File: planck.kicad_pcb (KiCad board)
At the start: 2 copper layers, 115 x 75 mm, 134 parts, among them J1 USB_C_U262-161N-4BVC11, J2 USB_C_U262-161N-4BVC11, J3 USB_C_U262-161N-4BVC11, SW1 SW_Hotswap_Kailh_Choc_V1_1u, SW10 SW_Hotswap_Kailh_Choc_V1_1u, SW11 SW_Hotswap_Kailh_Choc_V1_1u, SW12 SW_Hotswap_Kailh_Choc_V1_1u, SW13 SW_Hotswap_Kailh_Choc_V1_1u, SW14 SW_Hotswap_Kailh_Choc_V1_1u, SW15 SW_Hotswap_Kailh_Choc_V1_1u, SW16 SW_Hotswap_Kailh_Choc_V1_1u, SW17 SW_Hotswap_Kailh_Choc_V1_1u, SW18 SW_Hotswap_Kailh_Choc_V1_1u, SW19 SW_Hotswap_Kailh_Choc_V1_1u, SW2 SW_Hotswap_Kailh_Choc_V1_1u, SW20 SW_Hotswap_Kailh_Choc_V1_1u, SW21 SW_Hotswap_Kailh_Choc_V1_1u, SW22 SW_Hotswap_Kailh_Choc_V1_1u, SW23 SW_Hotswap_Kailh_Choc_V1_1u, SW24 SW_Hotswap_Kailh_Choc_V1_1u, SW25 SW_Push, SW3 SW_Hotswap_Kailh_Choc_V1_1u, SW4 SW_Hotswap_Kailh_Choc_V1_1u, SW5 SW_Hotswap_Kailh_Choc_V1_1u, SW6 SW_Hotswap_Kailh_Choc_V1_1u, SW7 SW_Hotswap_Kailh_Choc_V1_1u, SW8 SW_Hotswap_Kailh_Choc_V1_1u, SW9 SW_Hotswap_Kailh_Choc_V1_1u, U1 RP2040 ARM Cortex-M0 133MHz, U2 ME6219C33M5G, U3 W25Q16JVUXIQ, Y1 32MHz ±10ppm 20pF SMD3225-4P

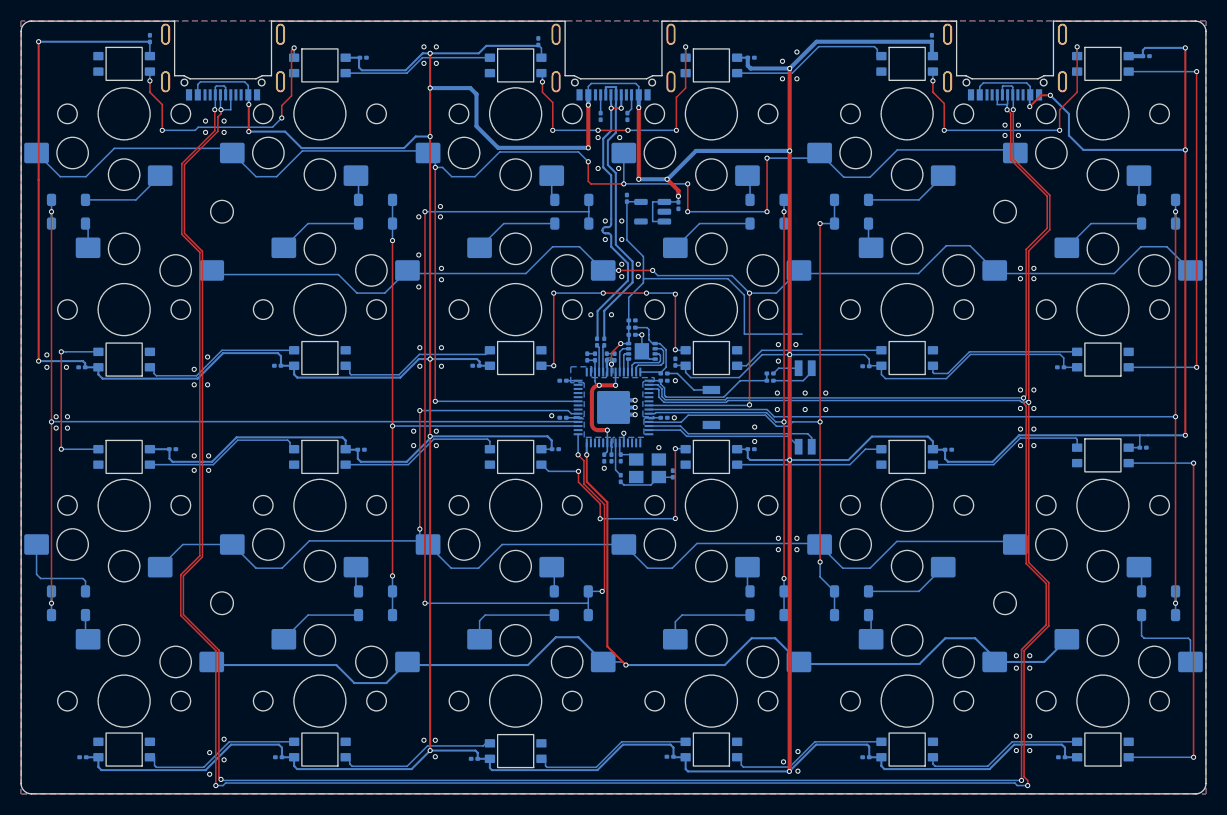
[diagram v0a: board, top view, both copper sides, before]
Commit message: connect LED, add case
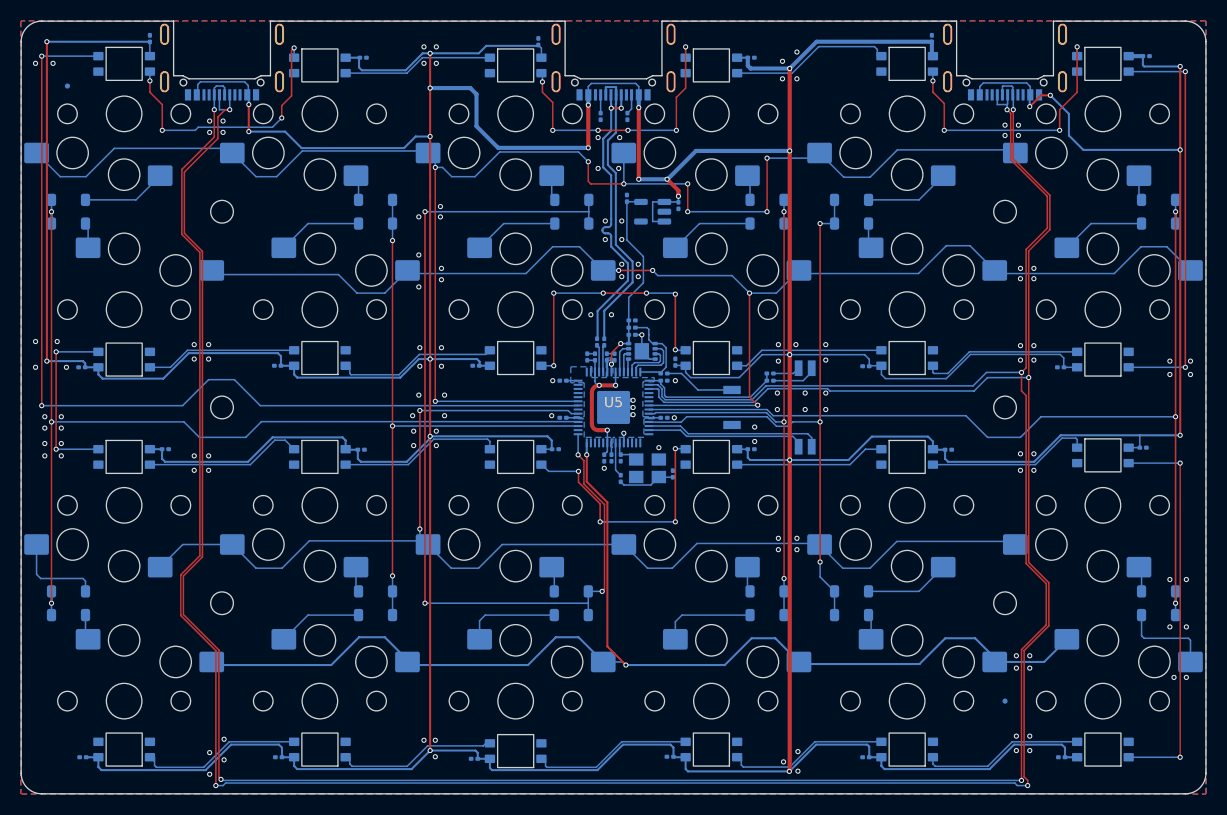
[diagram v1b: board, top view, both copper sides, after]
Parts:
- added FID1: Fiducial, Fiducial:Fiducial_0.5mm_Mask1.5mm, B.Cu at (86.0, 66.3)
- added FID2: Fiducial, Fiducial:Fiducial_0.5mm_Mask1.5mm, B.Cu at (177.0, 126.0)
- added H5: MountingHole, MountingHole:MountingHole_2.2mm_M2, F.Cu at (101.0, 97.5)
- added H6: MountingHole, MountingHole:MountingHole_2.2mm_M2, F.Cu at (177.0, 97.5)
- added U4: ~, MCU_RaspberryPi_and_Boards:bcase, B.Cu at (139.0, 97.5)
- added U5: tcase, MCU_RaspberryPi_and_Boards:tcase, F.Cu at (139.0, 97.5)
- SW26: value ~ -> DSHP02TSGET
- moved SW25 2.00 mm to (150.5, 97.5)
- moved C32 0.70 mm to (95.5, 101.5)
- moved J3 0.10 mm to (101.0, 64.3)
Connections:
- D25 pad 4: unconnected-(D25-DIN-Pad4) -> /LED
- U1 pad 36: unconnected-(U1-GPIO24-Pad36) -> /LED
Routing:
- net /LED: track 0.00 -> 93.6 mm, vias 0 -> 2
- net /V3V3: track 62.0 -> 42.1 mm
- net /VBUS: track 688.5 -> 683.9 mm
- net Net-(D42-DOUT): track 40.3 -> 37.7 mm
- net Net-(D30-DOUT): track 41.1 -> 38.9 mm
- net Net-(R9-Pad1): track 4.94 -> 6.94 mm
- net c6: track 96.3 -> 98.0 mm
- net /tx0: track 261.5 -> 263.1 mm
- net c1: track 96.0 -> 97.3 mm
- net r2: track 125.8 -> 127.0 mm
- net Net-(D36-DOUT): track 15.8 -> 16.8 mm
- net /rx0: track 264.9 -> 265.7 mm
- net r4: track 114.8 -> 115.6 mm
- net Net-(D35-DOUT): track 14.9 -> 14.3 mm
- net Net-(D39-DOUT): track 24.4 -> 25.1 mm
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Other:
- outline, holes or cut-outs redrawn
- board text added: "SL"
- board text added: "SR"
- board text added: "SWS"
- board text removed: "L/R"
- board text removed: "SERIAL"

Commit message: distance check add serial resistor for protection
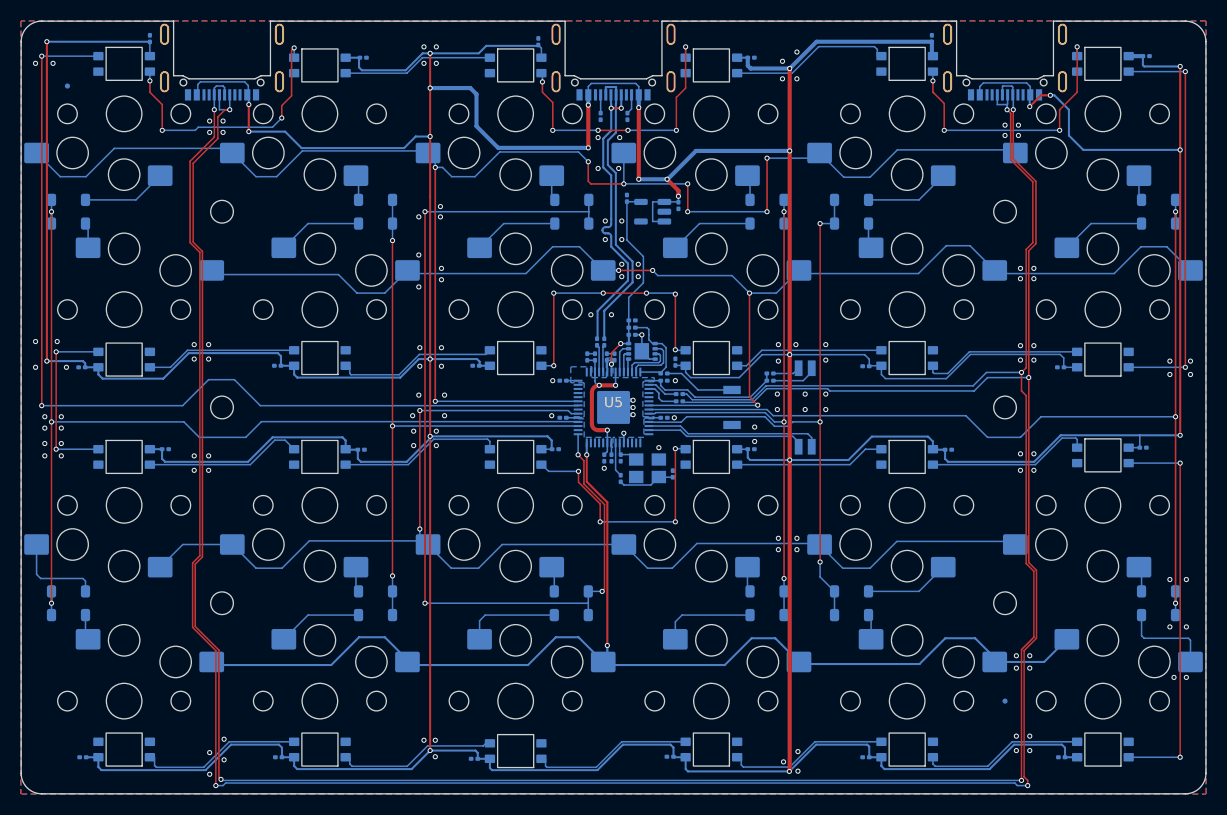
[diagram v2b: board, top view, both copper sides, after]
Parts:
- added R10: 27Ω ±1% 50mW 0201, Resistor_SMD:R_0201_0603Metric, B.Cu at (145.4, 96.2)
- added R11: 27Ω ±1% 50mW 0201, Resistor_SMD:R_0201_0603Metric, B.Cu at (145.4, 96.9)
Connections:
- U1 pad 2: /tx0 -> Net-(U1-GPIO0)
- U1 pad 3: /rx0 -> Net-(U1-GPIO1)
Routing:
- net /rx0: track 265.7 -> 257.8 mm
- net /tx0: track 263.1 -> 255.2 mm
- net Net-(U1-GPIO1): track 0.00 -> 3.43 mm
- net Net-(U1-GPIO0): track 0.00 -> 3.02 mm

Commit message: little  layout modification resistor over serial for protection  27R
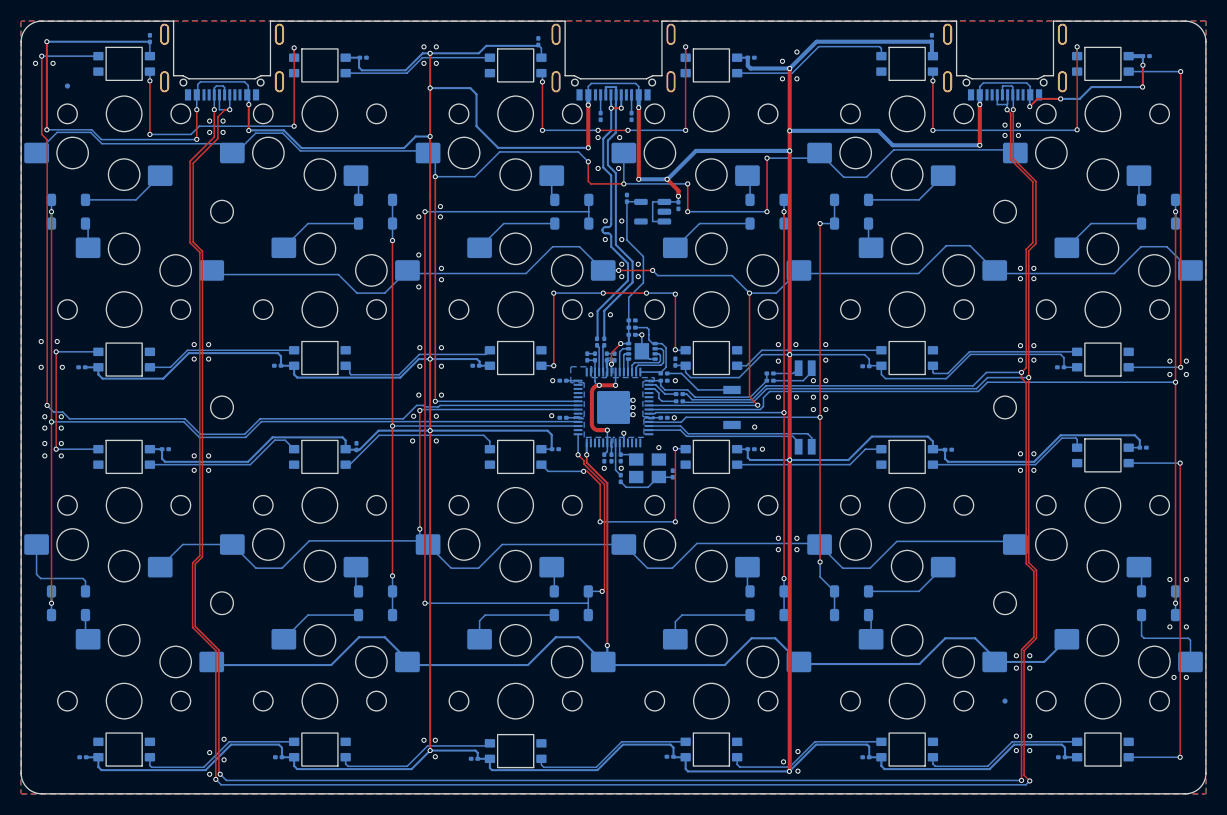
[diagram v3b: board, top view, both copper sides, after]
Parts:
- U4: value ~ -> bcase
- moved C25 0.54 mm to (114.0, 101.3), turned to -90 degrees
- moved R2 0.40 mm to (140.8, 69.2)
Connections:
- U1 pad 34: r3 -> unconnected-(U1-GPIO22-Pad34)
- U1 pad 35: unconnected-(U1-GPIO23-Pad35) -> r3
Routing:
- net /VBUS: track 684.1 -> 653.7 mm, vias 26 -> 30
- net Net-(D25-DOUT): track 26.5 -> 29.0 mm
- net Net-(D29-DOUT): track 27.1 -> 28.7 mm
- net r1: track 154.0 -> 152.5 mm
- net Net-(D27-DOUT): track 27.5 -> 28.6 mm
- net Net-(D47-DOUT): track 15.0 -> 15.9 mm
- net Net-(D46-DOUT): track 14.9 -> 15.7 mm
- net Net-(D42-DOUT): track 37.7 -> 38.5 mm
- net /rx0: track 257.8 -> 257.0 mm
- net Net-(D44-DOUT): track 15.0 -> 15.8 mm
- net Net-(D45-DOUT): track 15.0 -> 15.7 mm
- net Net-(D38-DOUT): track 15.5 -> 16.2 mm
- net c5: track 59.7 -> 59.1 mm
- net GND: vias 139 -> 140
